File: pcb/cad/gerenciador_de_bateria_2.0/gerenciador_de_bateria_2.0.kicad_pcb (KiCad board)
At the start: 2 copper layers, 40.1 x 32 mm, 35 parts, among them J1 Conn_01x01_Female, J2 Conn_01x01_Female, J3 Conn_01x01_Female, J4 Conn_01x01_Female, J5 Conn_01x02_Male, J6 Conn_01x01_Female, J7 Conn_01x01_Female, SW1 SW_Push, U1 MP2731, U2 USB_BQ25629

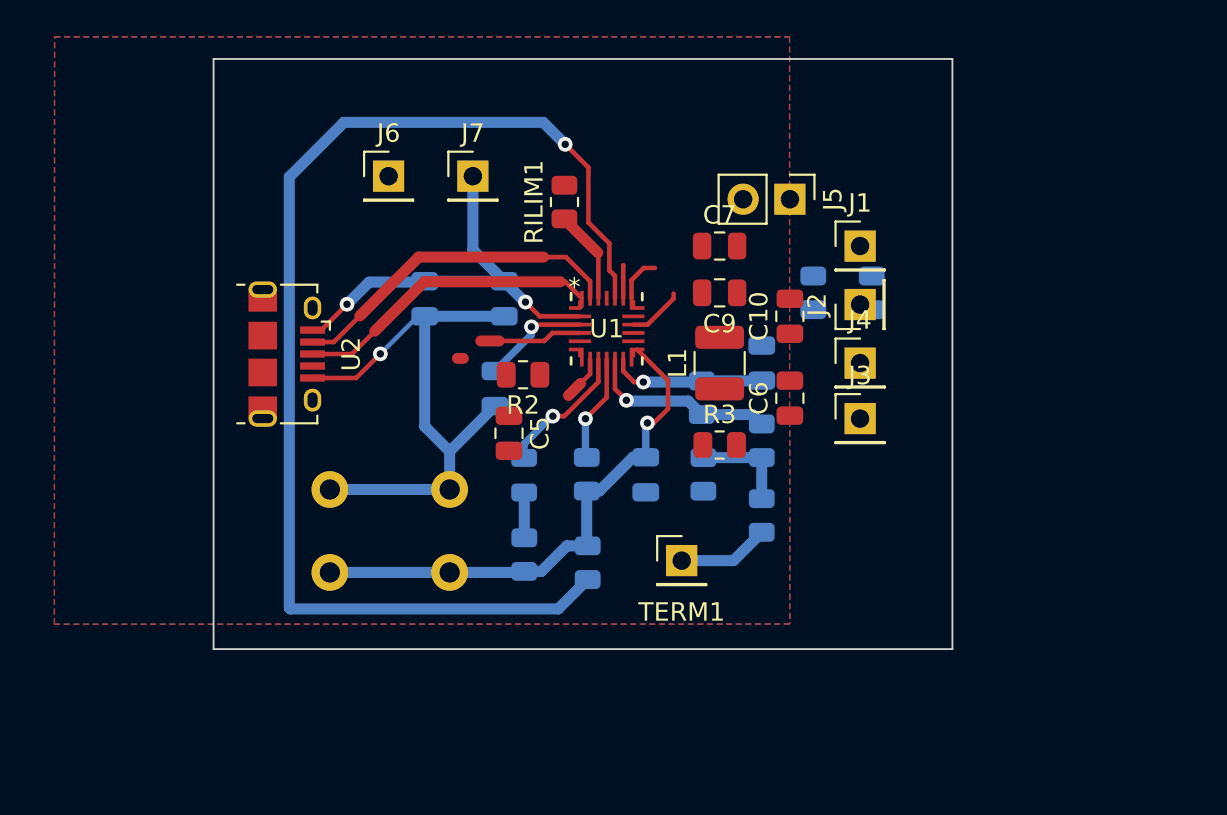
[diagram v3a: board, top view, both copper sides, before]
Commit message: Alterações no lauout de PCB do MP2731
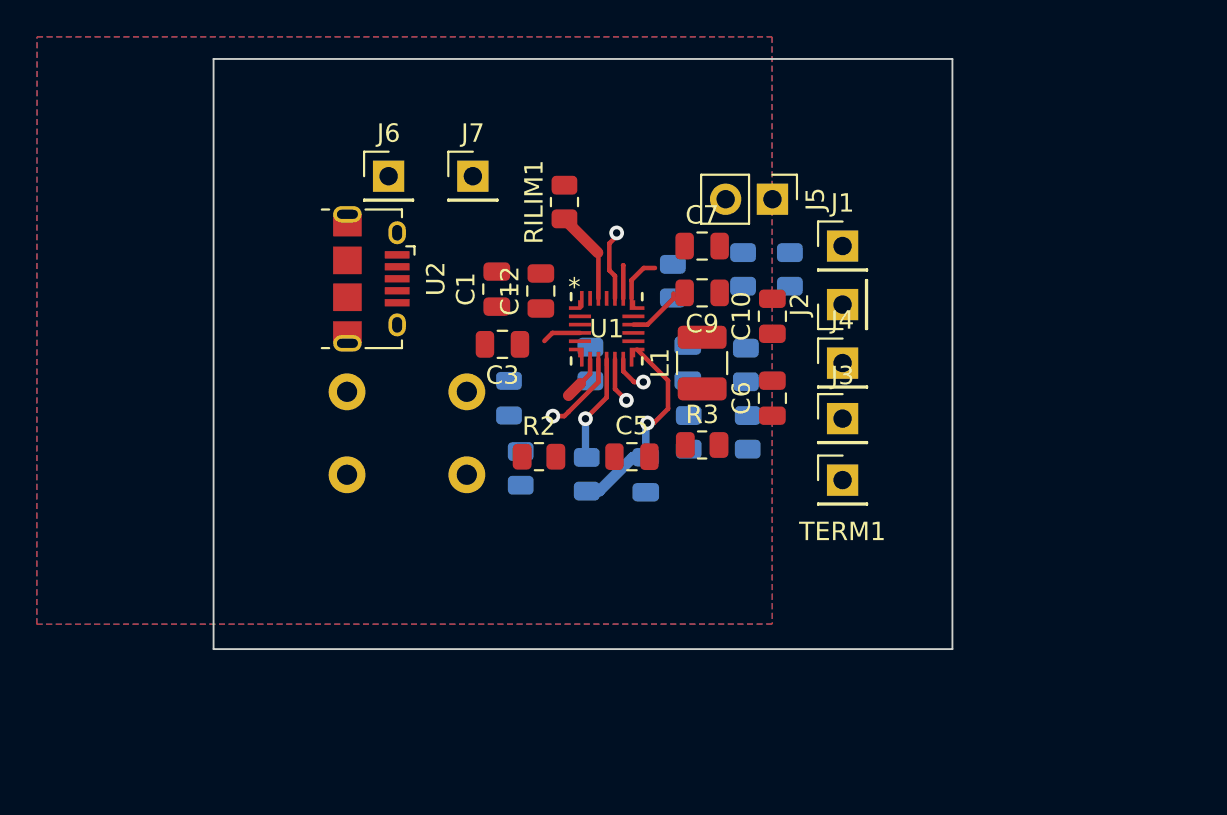
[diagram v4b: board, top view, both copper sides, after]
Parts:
- C1, C12, C3: moved to F.Cu
- moved R1 16.0 mm to (123.2, 120.0), turned to -90 degrees
- moved TERM1 9.76 mm to (132.4, 130.8)
- moved C5 6.79 mm to (121.0, 129.5), turned to 0 degrees
- moved R12 6.37 mm to (127.2, 124.6), turned to 90 degrees
- moved R6 6.31 mm to (118.7, 124.5)
- moved U2 6.14 mm to (106.8, 119.9)
- moved SW1 5.38 mm to (112.0, 126.0)
- moved R5 4.68 mm to (114.9, 130.2)
- moved R7 4.62 mm to (129.5, 119.4)
- moved R11 4.57 mm to (127.3, 128.2)
- moved R2 4.53 mm to (115.9, 129.5), turned to 0 degrees
- moved D1 4.26 mm to (114.3, 126.4)
- moved R8 4.02 mm to (127.0, 119.4)
- moved C11 4.01 mm to (124.0, 124.5)
- moved R4 3.99 mm to (124.1, 128.2)
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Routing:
- net Net-(R1-Pad1): track 66.4 -> 3.84 mm
- net GNDPWR: track 31.7 -> 0.00 mm, vias 1 -> 0
- net Net-(C12-Pad1): track 22.8 -> 0.00 mm, vias 2 -> 0
- net Net-(U1-Pad25): track 18.4 -> 0.00 mm
- net /VREF: track 29.1 -> 11.3 mm
- net Net-(U1-Pad26): track 16.6 -> 0.00 mm
- net Net-(R4-Pad1): track 10.4 -> 2.49 mm
- net Net-(C11-Pad2): track 8.44 -> 1.98 mm
- net Net-(C3-Pad1): track 5.90 -> 0.00 mm, vias 1 -> 0
- net Net-(R11-Pad2): track 5.40 -> 0.00 mm
- net Net-(TERM1-Pad1): track 4.98 -> 0.00 mm
- net Net-(C5-Pad2): track 5.88 -> 2.11 mm
- net Net-(D1-Pad1): track 7.42 -> 4.48 mm
- net Net-(D1-Pad2): track 2.46 -> 0.00 mm

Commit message: Atualização da placa para gerenciamento de bateria, finalização do layout e roteamento
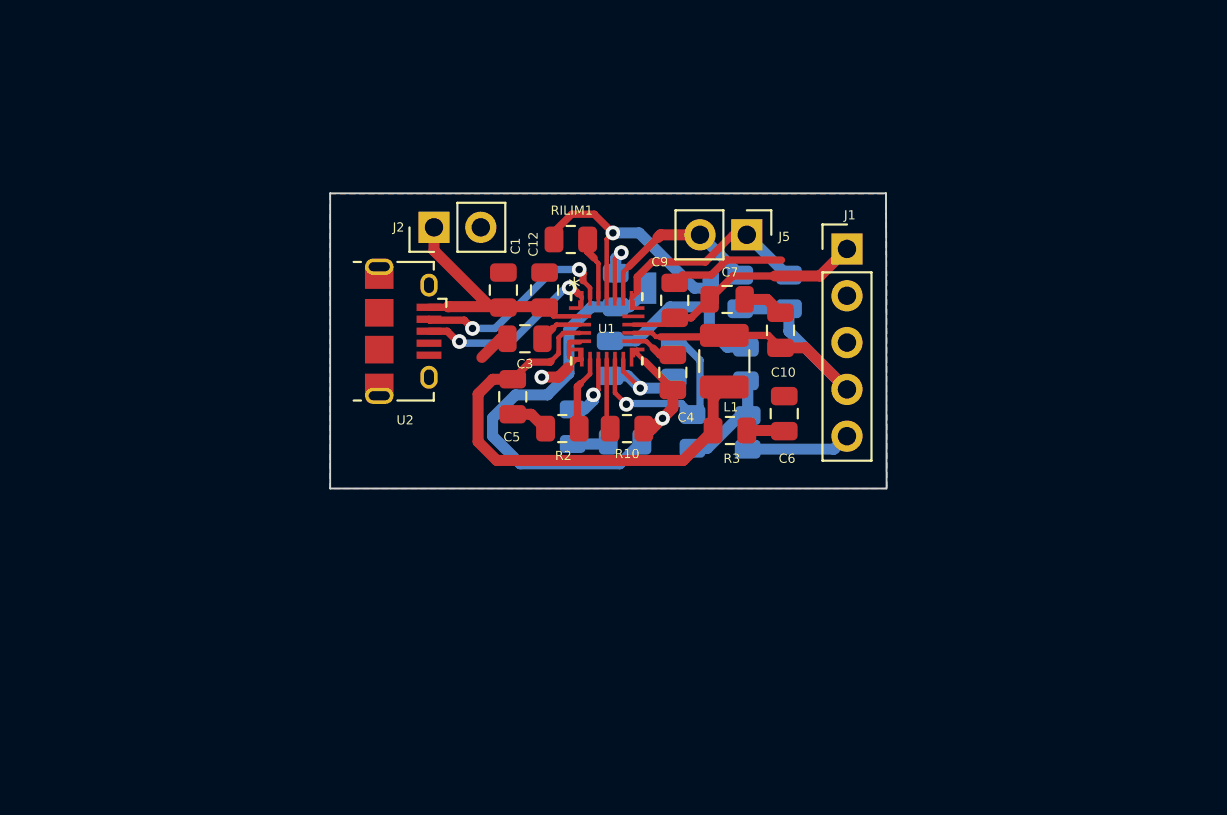
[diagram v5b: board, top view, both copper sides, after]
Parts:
- removed J3, J4, J6, J7, TERM1: Conn_01x01_Female, Connector_PinHeader_2.54mm:PinHeader_1x01_P2.54mm_Vertical
- C4, R10: moved to F.Cu
- J1: value Conn_01x01_Female -> Conn_01x05; footprint Connector_PinHeader_2.54mm:PinHeader_1x01_P2.54mm_Vertical -> Connector_PinHeader_2.54mm:PinHeader_1x05_P2.54mm_Vertical
- J2: value Conn_01x01_Female -> Conn_01x02; footprint Connector_PinHeader_2.54mm:PinHeader_1x01_P2.54mm_Vertical -> Connector_PinHeader_2.54mm:PinHeader_1x02_P2.54mm_Vertical
- SW1: footprint Button_Switch_THT:SW_PUSH_6mm -> Button_Switch_SMD:SW_SPST_B3U-1000P
- moved J2 22.6 mm to (110.2, 117.1)
- moved SW1 12.8 mm to (123.5, 120.4)
- moved C5 7.24 mm to (114.5, 126.3), turned to 90 degrees
- moved R5 5.85 mm to (120.6, 128.7), turned to 0 degrees
- moved C4 5.74 mm to (123.2, 125.0), turned to 90 degrees
- moved R6 4.52 mm to (123.2, 124.4), turned to 90 degrees
- moved C11 4.22 mm to (119.8, 124.2)
- moved D1 3.79 mm to (117.8, 127.9)
- moved U2 3.33 mm to (108.6, 122.7)
- moved R10 3.30 mm to (120.7, 128.0), turned to 180 degrees
- moved C7 3.20 mm to (126.1, 121.0)
- moved R1 3.14 mm to (120.1, 120.5)
- moved J5 2.38 mm to (127.2, 117.5)
- moved RILIM1 2.06 mm to (117.7, 117.8), turned to 180 degrees
- moved R2 1.98 mm to (117.2, 128.0), turned to 180 degrees
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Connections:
- net Net-(C7-Pad1) renamed /BATT
- C1 pad 1: Net-(C1-Pad1) -> /VIN
- C12 pad 1: Net-(C12-Pad1) -> /VIN
- J2 pad 1: GNDPWR -> /VIN
- R11 pad 1: Net-(TERM1-Pad1) -> /TERM
- U1 pad 2: Net-(C12-Pad1) -> /VIN
- U2 pad 1: Net-(C12-Pad1) -> /VIN
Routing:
- net GNDA: track 0.00 -> 27.9 mm, vias 0 -> 1
- net Net-(C5-Pad2): track 2.11 -> 26.5 mm
- net /SYS: track 0.01 -> 21.5 mm
- net /VREF: track 11.3 -> 30.9 mm
- net GNDPWR: track 0.00 -> 15.0 mm, vias 0 -> 1
- net /VIN: track 0.00 -> 14.0 mm
- net Net-(U1-Pad25): track 0.00 -> 11.5 mm, vias 0 -> 2
- net /BATT: track 3.04 -> 13.3 mm
- net Net-(U1-Pad26): track 0.00 -> 10.1 mm, vias 0 -> 2
- net Net-(R4-Pad1): track 2.49 -> 11.4 mm
- net /SCL: track 2.53 -> 11.4 mm
- net /SDA: track 1.80 -> 9.66 mm
- net /TERM: track 0.00 -> 5.68 mm
- net Net-(R11-Pad2): track 0.00 -> 5.66 mm
- net Net-(C11-Pad2): track 1.98 -> 5.91 mm
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- added copper zone on B.Cu, net GNDPWR
- added copper zone on F.Cu, net GNDPWR
- removed copper zone on B.Cu, net GNDA
- removed copper zone on F.Cu, net GNDA
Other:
- board size 40.1 x 32 mm -> 30.2 x 16 mm

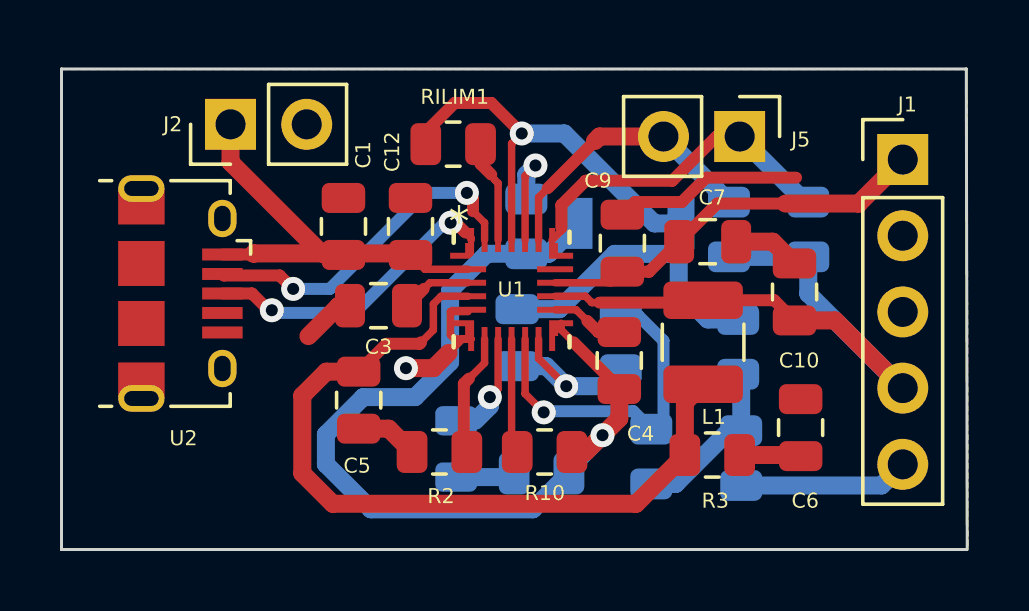
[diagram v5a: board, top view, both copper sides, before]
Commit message: Revisão da PCB do gerenciador de bateria 2.0, corrigindo os GND que estavam flutuando e atualizando footprint de componentes que estavam errados
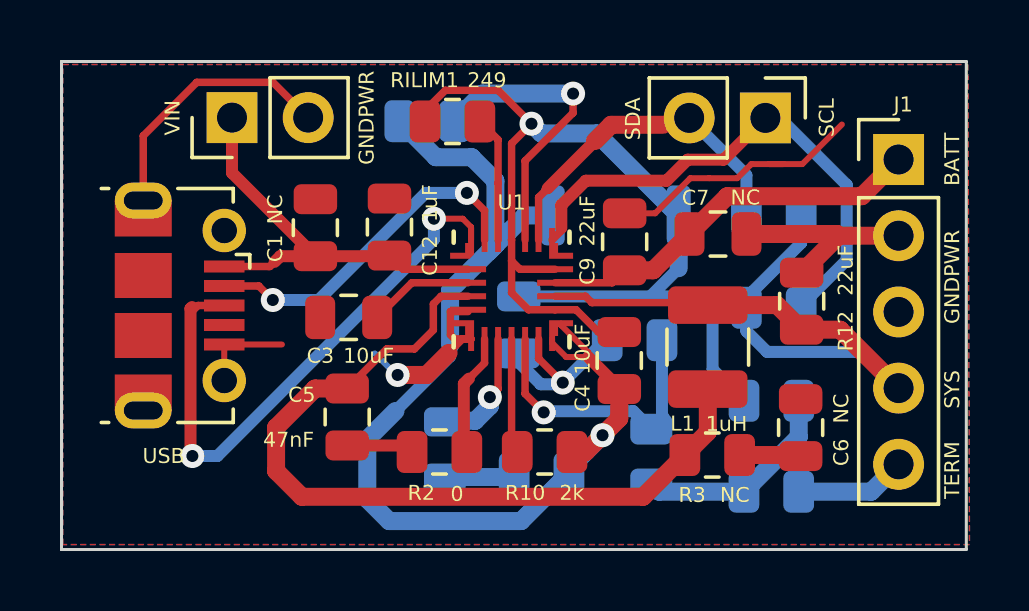
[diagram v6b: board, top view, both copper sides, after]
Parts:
- R12: renamed from C10; value 22uF -> (none)
- SW1: footprint Button_Switch_SMD:SW_SPST_B3U-1000P -> Button_Switch_SMD:SW_Push_SPST_NO_Alps_SKRK
- USB: renamed from U2; footprint Connector_USB:USB_Micro-B_Amphenol_10118194_Horizontal -> Connector_USB:USB_Micro-B_Molex-105017-0001
- moved R1 4.82 mm to (116.8, 117.0), turned to 180 degrees
- moved R7 2.85 mm to (128.3, 123.2), turned to 0 degrees
- moved R12 2.11 mm to (128.3, 126.3), turned to 180 degrees
- moved R8 1.56 mm to (128.3, 120.1), turned to 180 degrees
- moved R11 1.50 mm to (128.3, 129.3), turned to 180 degrees
- moved C3 1.07 mm to (114.2, 123.5)
- moved SDA 1.06 mm to (128.1, 116.9)
- moved C1 0.94 mm to (113.1, 120.5)
- moved RILIM1 0.75 mm to (117.6, 117.0)
- moved C12 0.70 mm to (115.5, 120.5)
- moved C5 0.68 mm to (114.1, 126.8)
- moved SW1 0.54 mm to (123.1, 120.1)
- moved R6 0.46 mm to (123.7, 124.3), turned to 0 degrees
- moved C11 0.43 mm to (119.8, 123.8)
- moved C7 0.43 mm to (126.5, 120.8)
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- renumbered J2 to GNDPWR, J5 to SDA
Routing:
- net GNDPWR: track 15.0 -> 33.9 mm
- net Net-(U1-Pad26): track 10.1 -> 24.7 mm
- net GNDA: track 27.9 -> 35.5 mm
- net /SCL: track 11.4 -> 17.7 mm
- net Net-(R1-Pad1): track 3.87 -> 9.87 mm
- net /VREF: track 30.9 -> 36.2 mm
- net /TERM: track 5.68 -> 3.71 mm
- net /SYS: track 21.5 -> 23.2 mm
- net Net-(R11-Pad2): track 5.66 -> 6.98 mm
- net Net-(R4-Pad1): track 11.4 -> 10.2 mm
- net Net-(D1-Pad1): track 3.04 -> 4.06 mm
- net /SDA: track 9.66 -> 10.6 mm
- net Net-(C5-Pad2): track 26.5 -> 27.2 mm
- net Net-(RILIM1-Pad1): track 3.55 -> 4.20 mm
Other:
- board size 30.2 x 16 mm -> 30.2 x 16.3 mm

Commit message: Atualização na PCB do gerenciador de bateria 2.0, após mais uma revisão para fabricação da placa, alterando apenas as identificações de cada componente, mantendo um padrão
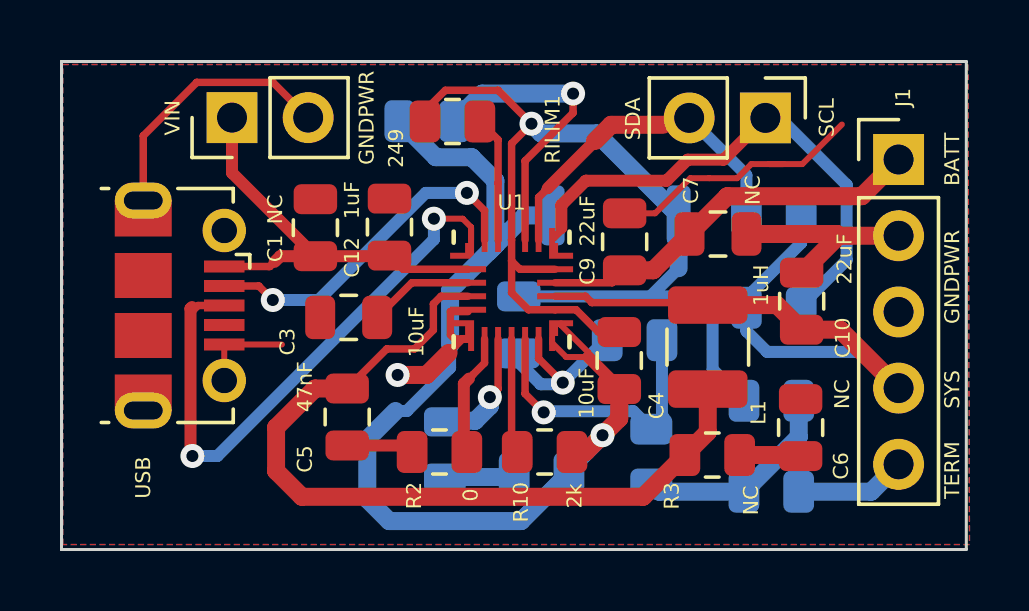
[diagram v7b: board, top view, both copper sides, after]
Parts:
- renumbered R12 to C10
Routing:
- net GNDPWR: track 33.9 -> 32.7 mm
